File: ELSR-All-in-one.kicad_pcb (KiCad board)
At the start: 4 copper layers, 91 x 45.5 mm, 92 parts, among them IC1 AT32F421K8U7, IC2 AT32F421K8U7, J1 Conn_01x05_Pin, J2 Conn_01x03_Pin, J3 Conn_01x03_Pin, J4 Conn_01x03_Pin, J5 Conn_01x03_Pin, J6 Conn_01x04_Pin, J7 Conn_01x04_Pin, J8 Conn_01x04_Socket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

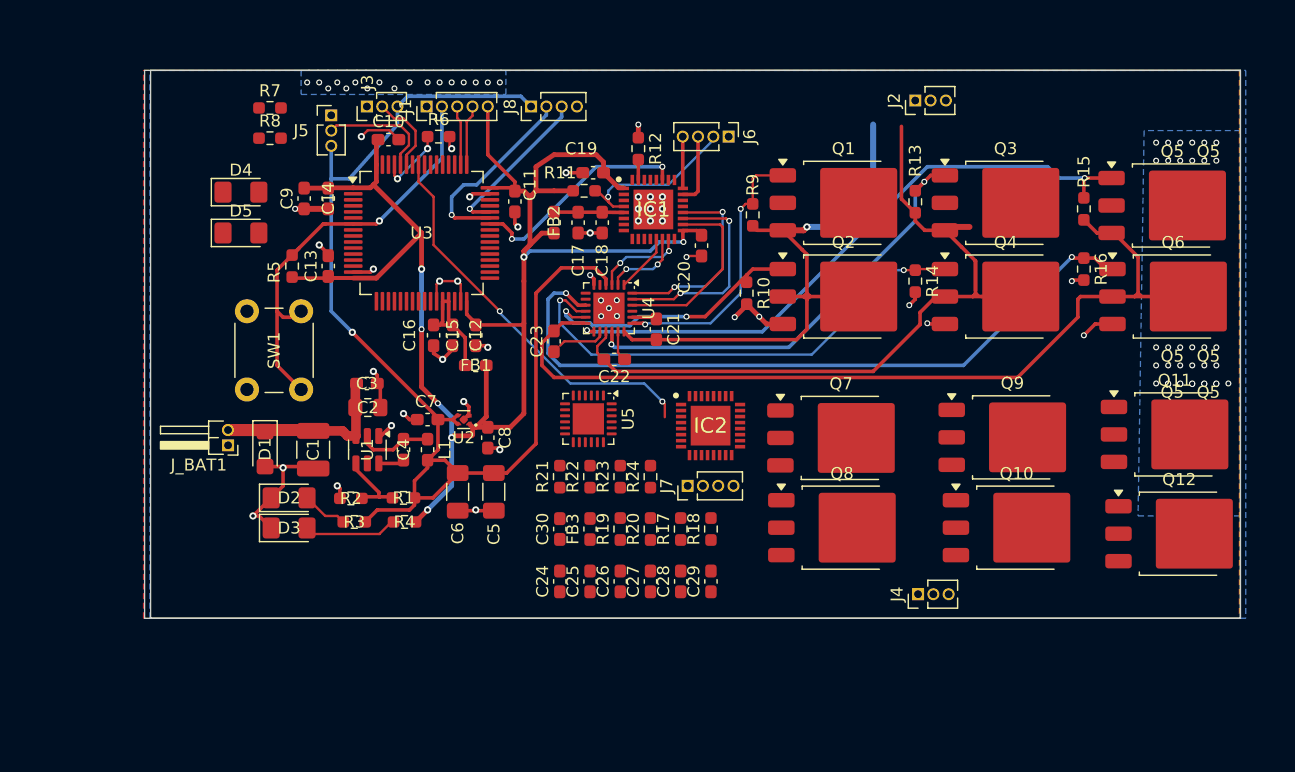
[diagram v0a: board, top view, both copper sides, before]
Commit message: updated to 4 layers and cleared several drc violations
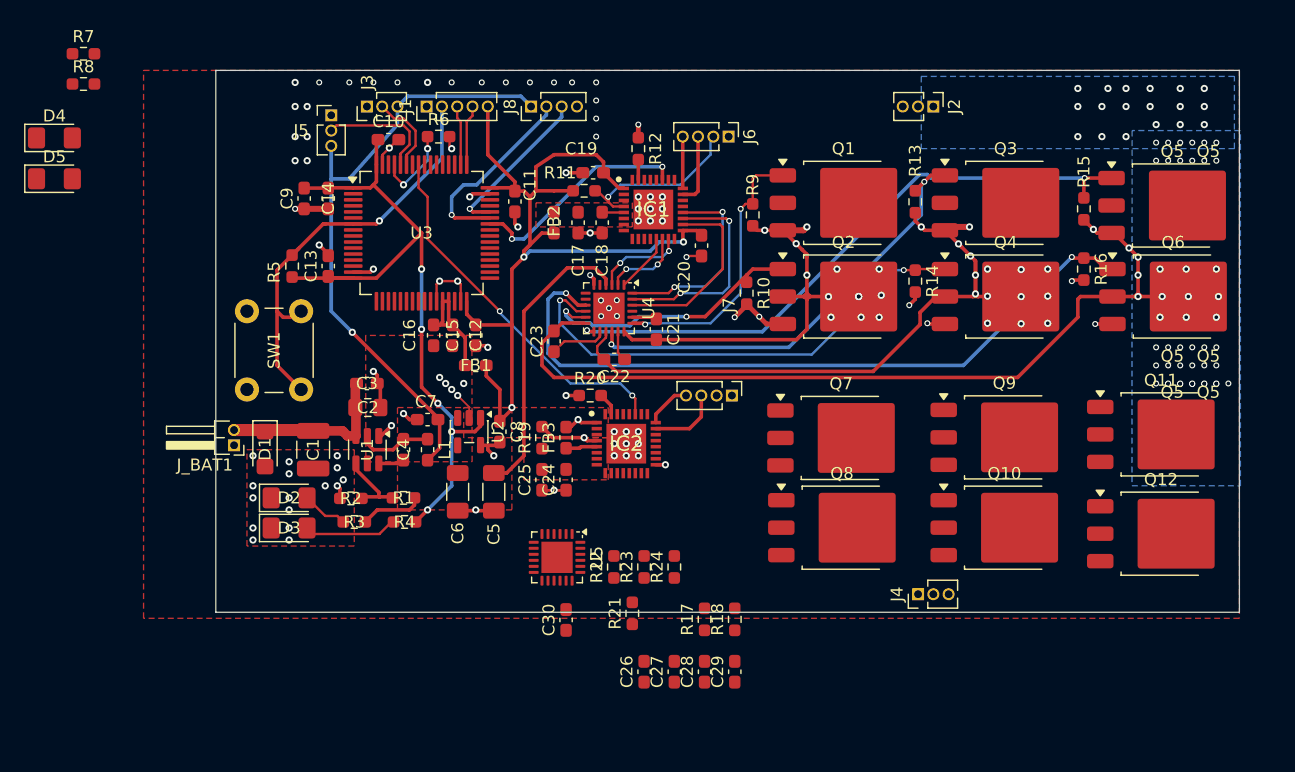
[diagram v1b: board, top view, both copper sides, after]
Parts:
- U2: footprint Package_SON:Texas_X2SON-4_1x1mm_P0.65mm -> Package_TO_SOT_SMD:SOT-23-5
- moved D4 16.1 mm to (15.5, 40.1)
- moved D5 16.1 mm to (15.5, 43.5)
- moved R7 16.1 mm to (17.9, 33.1)
- moved R8 16.1 mm to (17.9, 35.6)
- moved R21 12.8 mm to (63.5, 79.6)
- moved R20 12.2 mm to (60.0, 61.5), turned to 0 degrees
- moved U5 11.8 mm to (57.2, 74.9)
- moved R19 9.99 mm to (56.0, 65.0)
- moved C25 9.33 mm to (56.0, 68.5)
- moved C24 8.45 mm to (58.0, 68.5)
- moved J7 8.35 mm to (71.8, 61.5), turned to -90 degrees
- moved FB3 7.84 mm to (58.0, 65.0)
- moved C27 7.76 mm to (67.0, 84.4)
- moved R17 7.76 mm to (69.5, 80.1)
- moved C29 7.76 mm to (72.0, 84.4)
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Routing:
- net /ESC2/nrst: track 0.00 -> 17.5 mm, vias 0 -> 1
- net +5V: track 97.1 -> 80.6 mm
- net VDD: track 140.0 -> 155.2 mm, vias 7 -> 10
- net /ESC1/M_A: track 50.3 -> 37.9 mm, vias 1 -> 13
- net VSS: track 65.4 -> 56.3 mm, vias 45 -> 72
- net /ESC1/M_B: track 63.7 -> 56.1 mm, vias 0 -> 15
- net /ESC2/swdio: track 0.00 -> 5.96 mm
- net Net-(IC1-VDDA): track 5.80 -> 1.81 mm
- net /ESC2/swclk: track 0.00 -> 3.85 mm
- net Net-(IC2-VDDA): track 0.00 -> 2.60 mm
- net D_2: track 32.9 -> 30.5 mm
- net Net-(IC2-BOOT0): track 0.00 -> 1.90 mm
- net Net-(U3-PB8): track 5.81 -> 6.81 mm
- net V_BAT: track 18.4 -> 17.4 mm, vias 53 -> 58
- net /ESC1/G_CH: track 52.0 -> 51.4 mm
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- added copper zone on F.Cu, net +5V
- added copper zone on In2.Cu, net /ESC1/M_A
- added copper zone on In2.Cu, net /ESC1/M_B
- added copper zone on B.Cu, net /ESC1/M_C
- added copper zone on In2.Cu, net /ESC1/M_C
- added copper zone on F.Cu, net Net-(IC1-VDDA)
- added copper zone on F.Cu, net Net-(IC2-VDDA)
- added copper zone on F.Cu, net VDD
- added copper zone on F.Cu, net VSS
- added copper zone on In1.Cu, net VSS
- added copper zone on In2.Cu, net V_BAT
- removed copper zone on B.Cu, net VSS
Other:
- board size 91 x 45.5 mm -> 85 x 45 mm

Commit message: Almost Done
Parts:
- removed D4, D5: LED, LED_SMD:LED_1206_3216Metric_Pad1.42x1.75mm_HandSolder
- removed R7, R8: 150, Resistor_SMD:R_0603_1608Metric_Pad0.98x0.95mm_HandSolder
- moved R23 37.6 mm to (100.5, 65.0), turned to -90 degrees
- moved R24 33.6 mm to (100.5, 73.0), turned to -90 degrees
- moved R21 27.7 mm to (87.0, 65.0), turned to -90 degrees
- moved R22 25.3 mm to (87.0, 72.0), turned to -90 degrees
- moved C27 23.9 mm to (57.5, 62.5), turned to 0 degrees
- moved C26 16.8 mm to (67.8, 68.0), turned to 0 degrees
- moved R17 14.9 mm to (72.5, 65.5), turned to -90 degrees
- moved C29 14.8 mm to (58.5, 78.5), turned to 180 degrees
- moved C28 11.6 mm to (61.5, 76.0), turned to -90 degrees
- moved R18 7.65 mm to (73.0, 72.5), turned to -90 degrees
- moved C30 4.79 mm to (54.0, 77.5)
- moved J4 3.26 mm to (88.5, 81.0), turned to -90 degrees
- moved R20 1.59 mm to (61.6, 61.5)
- moved U5 0.97 mm to (57.9, 74.2)
- moved Q11 0.66 mm to (108.1, 64.7)
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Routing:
- net /ESC2/M_C: track 0.00 -> 83.0 mm, vias 0 -> 7
- net /ESC2/M_B: track 0.00 -> 56.3 mm, vias 0 -> 8
- net /ESC2/G_CL: track 0.00 -> 55.2 mm, vias 0 -> 2
- net /ESC2/G_CH: track 0.00 -> 54.7 mm, vias 0 -> 2
- net /ESC2/M_A: track 0.00 -> 39.8 mm, vias 0 -> 8
- net /ESC2/G_BL: track 0.00 -> 39.7 mm, vias 0 -> 2
- net /ESC2/G_BH: track 0.00 -> 38.3 mm, vias 0 -> 2
- net /ESC2/G_AL: track 0.00 -> 25.8 mm, vias 0 -> 2
- net /ESC2/G_AH: track 0.00 -> 22.3 mm, vias 0 -> 2
- net /ESC2/C_HIGH: track 0.00 -> 19.4 mm
- net /ESC2/A_HIGH: track 0.00 -> 17.3 mm, vias 0 -> 2
- net /ESC2/B_HIGH: track 0.00 -> 16.6 mm, vias 0 -> 2
- net VSS: track 56.3 -> 72.7 mm, vias 72 -> 68
- net /ESC2/C_LOW: track 0.00 -> 10.1 mm, vias 0 -> 2
- net /ESC2/B_LOW: track 0.00 -> 7.92 mm, vias 0 -> 2
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- added copper zone on B.Cu, net /ESC1/M_A
- added copper zone on B.Cu, net /ESC1/M_B
- added copper zone on In1.Cu, net /ESC1/M_C
- added copper zone on B.Cu, net /ESC2/M_A
- added copper zone on In2.Cu, net /ESC2/M_A
- added copper zone on B.Cu, net /ESC2/M_B
- added copper zone on In2.Cu, net /ESC2/M_B
- added copper zone on B.Cu, net /ESC2/M_C
- added copper zone on F.Cu, net /ESC2/M_C
- added copper zone on In1.Cu, net /ESC2/M_C
- added copper zone on In1.Cu, net V_BAT
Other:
- board size 85 x 45 mm -> 85 x 50 mm

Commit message: Updated PCB Design and footprints
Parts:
- BATTERY: renamed from J_BAT1; footprint Connector_PinHeader_1.27mm:PinHeader_1x02_P1.27mm_Horizontal -> Connector_Wire:SolderWire-1.5sqmm_1x02_P6mm_D1.7mm_OD3mm
- M1: renamed from J2; footprint Connector_PinHeader_1.27mm:PinHeader_1x03_P1.27mm_Vertical -> Connector_Wire:SolderWire-2sqmm_1x03_P7.8mm_D2mm_OD3.9mm
- M2: renamed from J4; footprint Connector_PinHeader_1.27mm:PinHeader_1x03_P1.27mm_Vertical -> Connector_Wire:SolderWire-2sqmm_1x03_P7.8mm_D2mm_OD3.9mm
- W1: renamed from J3; footprint Connector_PinHeader_1.27mm:PinHeader_1x03_P1.27mm_Vertical -> Connector_PinHeader_2.54mm:PinHeader_1x03_P2.54mm_Vertical
- W2: renamed from J5; footprint Connector_PinHeader_1.27mm:PinHeader_1x03_P1.27mm_Vertical -> Connector_PinHeader_2.54mm:PinHeader_1x03_P2.54mm_Vertical
- moved M2 11.8 mm to (100.3, 81.5), turned to 180 degrees
- moved M1 10.3 mm to (98.8, 38.0), turned to 180 degrees
- moved W2 9.70 mm to (33.5, 46.5), turned to 180 degrees
- moved BATTERY 6.39 mm to (31.0, 72.0), turned to 90 degrees
- moved W1 4.00 mm to (37.5, 37.5)
- moved D1 2.07 mm to (35.0, 66.5)
- moved D2 1.41 mm to (36.0, 71.0)
- moved D3 1.41 mm to (36.0, 73.5)
- moved C1 1.12 mm to (38.0, 66.5)
- moved R2 0.28 mm to (40.4, 70.0)
- renumbered J6 to ESC1, J7 to ESC2, J8 to Reciever, J1 to STM32
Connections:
- W1 pad 1: VSS -> W1_PWM
- W1 pad 2: W1_PWM -> +5V
- W1 pad 3: +5V -> VSS
- W2 pad 2: W2_PWM -> +5V
- W2 pad 3: +5V -> W2_PWM
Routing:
- net V_BAT: track 17.4 -> 0.00 mm
- net /ESC2/M_C: track 83.0 -> 74.6 mm, vias 7 -> 8
- net +5V: track 88.5 -> 96.3 mm
- net VSS: track 72.7 -> 79.7 mm, vias 68 -> 51
- net W1_PWM: track 6.73 -> 11.3 mm, vias 0 -> 1
- net Net-(U3-PB8): track 6.81 -> 10.9 mm
- net W2_PWM: track 9.95 -> 13.8 mm, vias 0 -> 1
- net /ESC1/G_CL: track 57.8 -> 61.5 mm
- net nrst: track 35.8 -> 37.5 mm
- net Net-(D2-A): track 3.84 -> 2.43 mm
- net /ESC1/G_BL: track 40.4 -> 41.4 mm
- net Net-(D3-A): track 7.81 -> 6.81 mm
- net /ESC1/M_A: track 37.9 -> 37.1 mm, vias 19 -> 18
- net Net-(U4-VB3): track 4.05 -> 4.76 mm
- net /ESC2/G_CL: track 55.2 -> 55.8 mm
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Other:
- board text added: "+"
- board text added: "+5V"
- board text added: "-"
- board text added: "3.3V"
- board text added: "CLK"
- board text added: "GND"
- board text added: "IO"
- board text added: "RAILSIDE ROBOTICS @PURDUE"
- board text added: "RST"
- board text added: "RX"
- board text added: "S"
- board text added: "TX"
- board text removed: "Q5"

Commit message: Updates
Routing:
- net /ESC2/M_C: track 74.6 -> 73.4 mm
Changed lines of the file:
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@@
 	)
 	(segment
-		(start 82 79.5)
-		(end 55 79.5)
+		(start 53.543748 78.043748)
+		(end 52.5 77)
 		(width 0.4)
 		(layer "In1.Cu")
@@
 	(segment
 		(start 104.5 78.5)
-		(end 104 78)
+		(end 104.043748 78.043748)
 		(width 0.4)
 		(layer "In1.Cu")
@@
 	)
 	(segment
-		(start 104 78)
-		(end 83.5 78)
+		(start 104.043748 78.043748)
+		(end 53.543748 78.043748)
 		(width 0.4)
 		(layer "In1.Cu")
-		(net "/ESC2/M_C")
-	)
-	(segment
-		(start 55 79.5)
-		(end 52.5 77)
-		(width 0.4)
-		(layer "In1.Cu")
-		(net "/ESC2/M_C")
-	)
-	(segment
-		(start 83.5 78)
-		(end 82 79.5)
-		(width 0.4)
-		(layer "In1.Cu")
